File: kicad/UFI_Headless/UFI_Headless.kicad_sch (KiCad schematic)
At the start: 0 parts

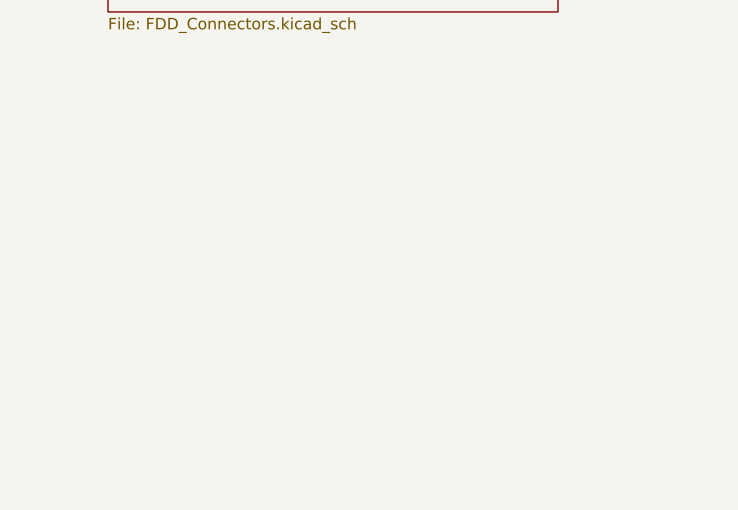
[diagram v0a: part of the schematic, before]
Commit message: KiCad v0.7 rework, schematic stage A6 with the matching firmware pin map: W5500 LAN bridge on a new sheet LAN - U23 WIZnet W5500 (LQFP-48) on SPI3 of the H723 (PC10 SCLK, PC11 MISO, PC12 MOSI, PA15 SCSn, PD5 INTn, PD10 RSTn; SPI3 pin mapping verified against the ST pin database via the embassy stm32h723zg tables, 10k pull-ups R119-R121), J22 HanRun HR911105A RJ45 with integrated 1CT:1CT magnetics, internal Bob-Smith network and LEDs (pinout from the HanRun datasheet rev. A/2 fetched from LCSC: 1 TD+, 2 TD-, 3 RD+, 4 TX centre tap, 5 RX centre tap, 6 RD-, 7 NC, 8 CHS GND to PCB ground per HanRun note, 9/10 green LED = LINK, 12/11 yellow LED = ACT via R117/R118 330 R, shield to GND); analogue front end taken from the WIZnet reference schematic W5500-Ref-ExternalMag (2015) and the W5500 datasheet v1.1.0: R112/R113 49.9 R 1% TXP/TXN to 3V3A, R114 10 R + C71 22 nF on the TX centre tap, C72/C73 6.8 nF series on RXP/RXN with R115/R116 82 R to the RX centre tap and C74 10 nF, R111 12.4k 1% on EXRES1, C61 10 nF on 1V2O, C62 4.7 uF on TOCAP, VBG left open, RSVD 23 to GND, RSVD 38-42 open (no-connect flags), PMODE0-2 through R122-R124 10k to +3V3 (all capable, auto-negotiation), Y2 25 MHz (same crystal as Y1) with C59/C60 18 pF and R109 1M, 3V3A behind FB2 600R@100MHz with C63 10 uF + C64-C68 100 nF, VDD with C69 10 uF + C70 100 nF, PWR_FLAG on 3V3A; sheet note with the sources. MCU_Core: six no-connect flags removed, global labels LAN_SCK/MISO/MOSI/CS/INT/RST on U5; root sheet LAN added as page 8. ERC over the whole project 0 errors / 0 warnings; netlist against the firmware pin table: all 61 entries match. Firmware (same commit): board.h externs PIN_LAN_SCK/MISO/MOSI/CS/INT/RST and LAN_SPI_AF = AF6, board_headless.c pin table and reset-safe init (GPIOC clock enabled, RST held low so the W5500 stays in reset until a driver exists, CS high, SPI pins and INT plain inputs); no protocol change. Docs: PLAN.md row A6 done, kicad README (LAN row in the v1.0 table, GPIO table), desig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
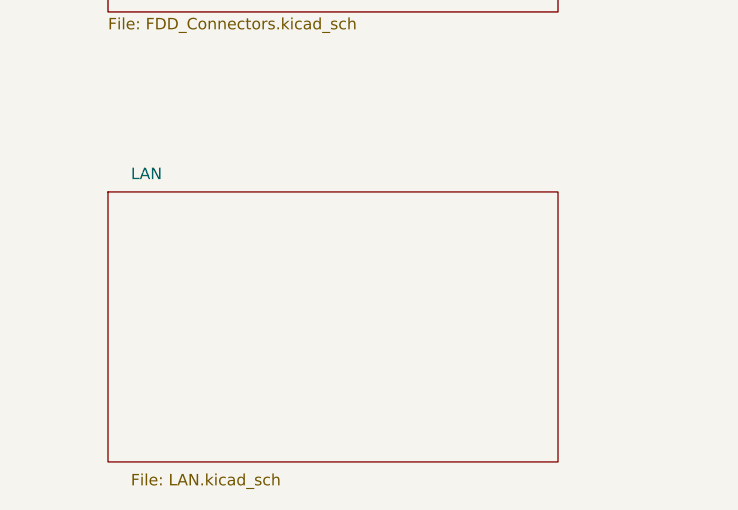
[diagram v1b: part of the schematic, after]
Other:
- added sheet LAN (LAN.kicad_sch)
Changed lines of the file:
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@@
 (sheet (at 120 100) (size 50 30) (fields_autoplaced yes) (stroke (width 0.1524) (type solid)) (fill (color 0 0 0 0.0000)) (property "Sheetname" "IEC_Bus" (at 120 99.3 0) (effects (font (size 1.27 1.27)) (justify left bottom))) (property "Sheetfile" "IEC_Bus.kicad_sch" (at 120 130.6 0) (effects (font (size 1.27 1.27)) (justify left top))) (instances (project "UFI_Headless" (path "/dc1b800d-cedf-5627-97f0-e6992ff33669" (page "6")))))
 (sheet (at 210 100) (size 50 30) (fields_autoplaced yes) (stroke (width 0.1524) (type solid)) (fill (color 0 0 0 0.0000)) (property "Sheetname" "Apple_Port" (at 210 99.3 0) (effects (font (size 1.27 1.27)) (justify left bottom))) (property "Sheetfile" "Apple_Port.kicad_sch" (at 210 130.6 0) (effects (font (size 1.27 1.27)) (justify left top))) (instances (project "UFI_Headless" (path "/dc1b800d-cedf-5627-97f0-e6992ff33669" (page "7")))))
+  (sheet (at 30.0 150.0) (size 50.0 30.0) (fields_autoplaced yes)
+    (stroke (width 0.0006) (type default))
+    (fill (color 0 0 0 0.0000))
+    (property "Sheetname" "LAN" (at 32.54 148.73 0)
+      (effects (font (size 1.27 1.27)) (justify left bottom))
+    )
+    (property "Sheetfile" "LAN.kicad_sch" (at 32.54 181.27 0)
+      (effects (font (size 1.27 1.27)) (justify left top))
+    )
+    (instances
+      (project "UFI_Headless"
+        (path "/dc1b800d-cedf-5627-97f0-e6992ff33669" (page "8"))
+      )
+    )
+  )
 (sheet_instances (path "/" (page "1")))
 )
